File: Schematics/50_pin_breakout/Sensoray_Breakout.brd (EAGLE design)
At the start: 96.2 x 43.8 mm, 26 parts, among them X1 87758-5016

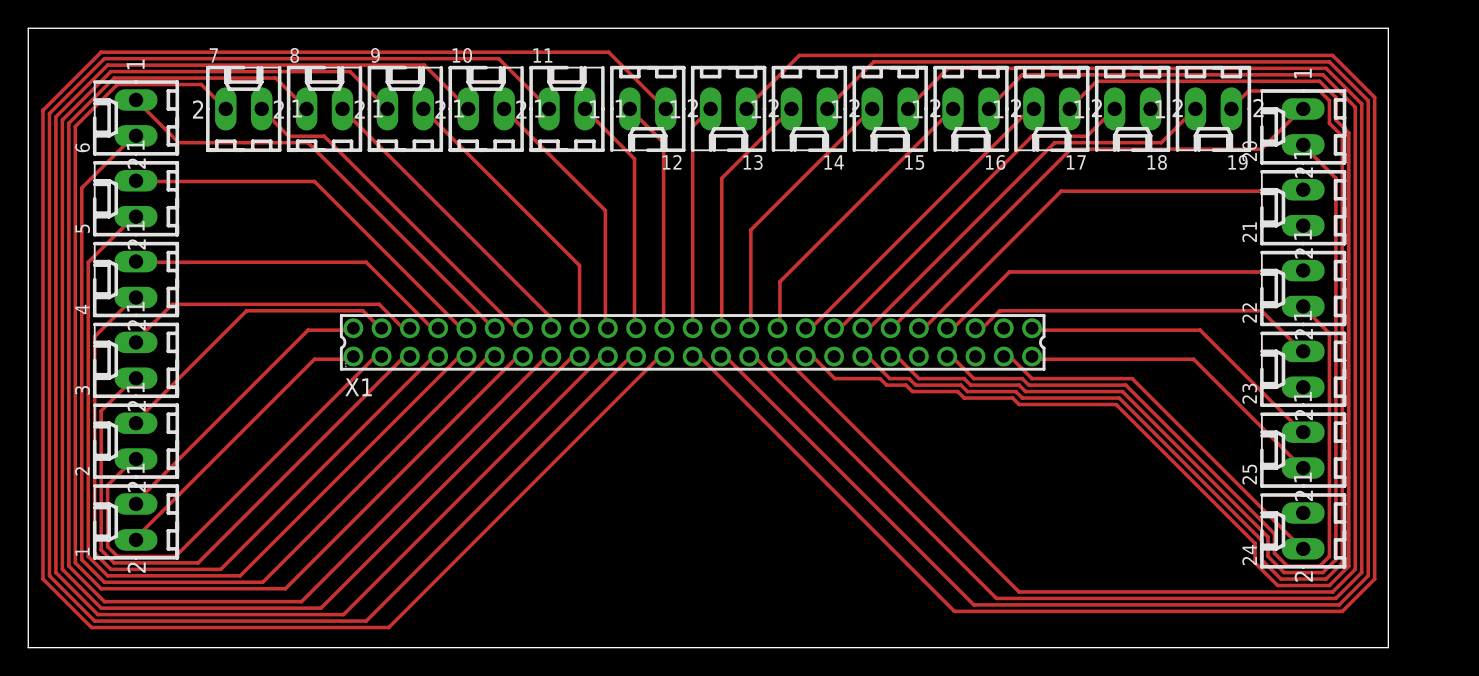
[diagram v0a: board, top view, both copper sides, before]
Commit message: added Rev 2 for 26 and 50 pin breakout boards, along with their gerber files for 1-layer PCB use. also added WPR for week of 27th
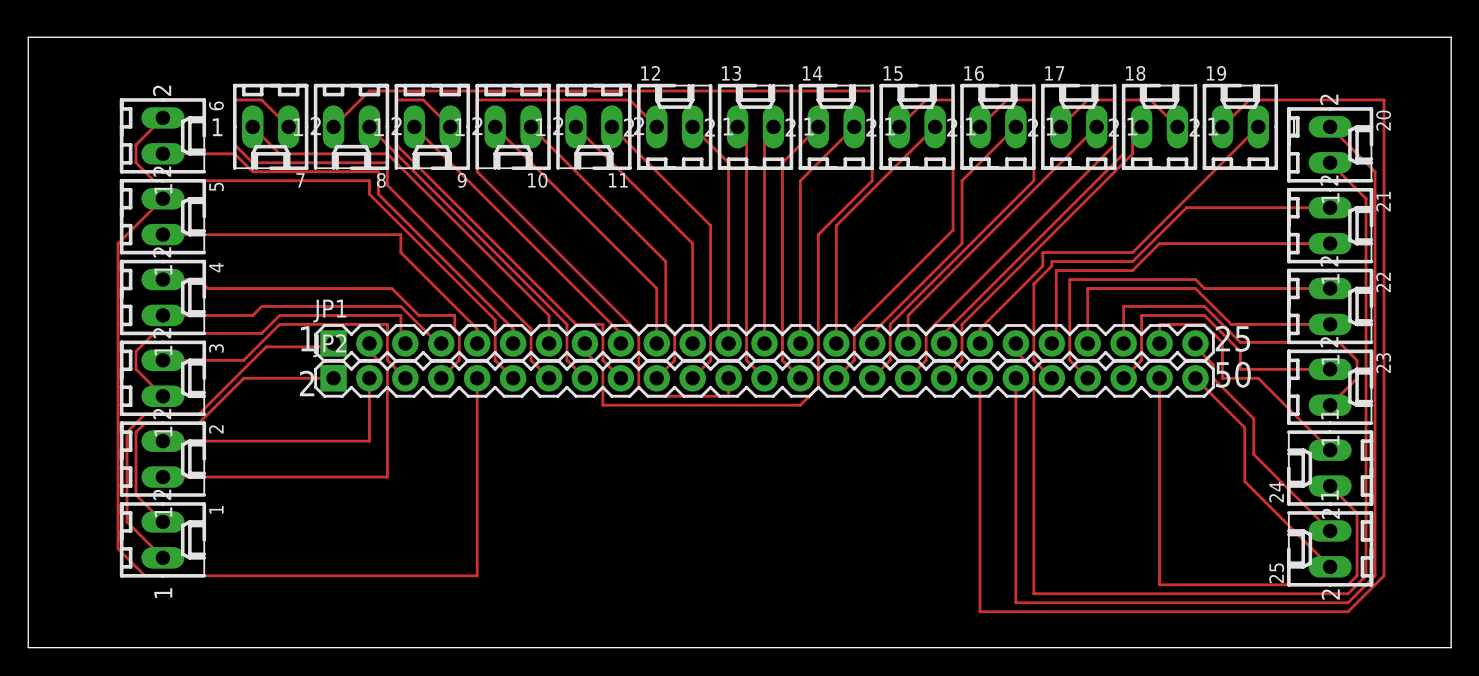
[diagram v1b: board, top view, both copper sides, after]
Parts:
- removed X1: 87758-5016, con-molex:87758-5016
- added JP1, JP2: M25PTH, SparkFun-Connectors:1X25
- moved 25 7.24 mm to (92.1, 6.99)
- moved 24 4.84 mm to (92.1, 12.7)
- moved 10 2.29 mm to (34.3, 36.8), turned to 180 degrees
- moved 11 2.29 mm to (40.0, 36.8), turned to 180 degrees
- moved 12 2.29 mm to (45.7, 36.8), turned to 0 degrees
- moved 13 2.29 mm to (51.4, 36.8), turned to 0 degrees
- moved 14 2.29 mm to (57.1, 36.8), turned to 0 degrees
- moved 15 2.29 mm to (62.9, 36.8), turned to 0 degrees
- moved 16 2.29 mm to (68.6, 36.8), turned to 0 degrees
- moved 17 2.29 mm to (74.3, 36.8), turned to 0 degrees
- moved 18 2.29 mm to (80.0, 36.8), turned to 0 degrees
- moved 19 2.29 mm to (85.7, 36.8), turned to 0 degrees
- moved 8 2.29 mm to (22.9, 36.8), turned to 180 degrees
- moved 6 2.29 mm to (9.53, 36.2), turned to 270 degrees
- moved 21 2.29 mm to (92.1, 29.8), turned to 270 degrees
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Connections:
- net N$1: now also 1.1, JP1.1; no longer 1.2, X1.1
- net N$10: now also 9.1, JP1.9; no longer 8.2, X1.15
- net N$11: now also 25.1, JP1.25; no longer 9.2, X1.17
- net N$12: now also 24.1, JP1.24; no longer 10.2, X1.19
- net N$13: now also 23.1, JP1.23; no longer 11.2, X1.21
- net N$14: now also 22.1, JP1.22; no longer 12.2, X1.23
- net N$15: now also 21.1, JP1.21; no longer 13.2, X1.25
- net N$16: now also 20.1, JP1.20; no longer 3.1, X1.6
- net N$17: now also 19.1, JP1.19; no longer 4.1, X1.8
- net N$18: now also 18.1, JP1.18; no longer 5.1, X1.10
- net N$19: now also 17.1, JP1.17; no longer 6.1, X1.12
- net N$2: now also 2.1, JP1.2; no longer 1.1, X1.2
- net N$20: now also 16.1, JP1.16; no longer 7.1, X1.14
- net N$21: now also 15.1, JP1.15; no longer 8.1, X1.16
- net N$22: now also 14.1, JP1.14; no longer 9.1, X1.18
- net N$23: now also 13.1, JP1.13; no longer 10.1, X1.20
- net N$24: now also 12.1, JP1.12; no longer 11.1, X1.22
- net N$25: now also 11.1, JP1.11; no longer 12.1, X1.24
- net N$26: now also 10.1, JP1.10; no longer 13.1, X1.26
- net N$27: now also 1.2, JP2.1; no longer 14.2, X1.27
- net N$28: now also 3.2, JP2.3; no longer 15.2, X1.29
- net N$29: now also 4.2, JP2.4; no longer 16.2, X1.31
- net N$3: now also JP2.2; no longer X1.3
- net N$30: now also 5.2, JP2.5; no longer 17.2, X1.33
- net N$31: now also 6.2, JP2.6; no longer 18.2, X1.35
- net N$32: now also 7.2, JP2.7; no longer 19.2, X1.37
- net N$33: now also 8.2, JP2.8; no longer 20.2, X1.39
- net N$34: now also 9.2, JP2.9; no longer 21.2, X1.41
- net N$35: now also 10.2, JP2.10; no longer 22.2, X1.43
- net N$36: now also 11.2, JP2.11; no longer 23.2, X1.45
- net N$37: now also 12.2, JP2.12; no longer 24.2, X1.47
- net N$38: now also 13.2, JP2.13; no longer 25.2, X1.49
- net N$39: now also 14.2, JP2.14; no longer 14.1, X1.28
- net N$4: now also 3.1, JP1.3; no longer 2.1, X1.4
- net N$40: now also 15.2, JP2.15; no longer 15.1, X1.30
- net N$41: now also 16.2, JP2.16; no longer 16.1, X1.32
- net N$42: now also 17.2, JP2.17; no longer 17.1, X1.34
- net N$43: now also 18.2, JP2.18; no longer 18.1, X1.36
- net N$44: now also 19.2, JP2.19; no longer 19.1, X1.38
- net N$45: now also 20.2, JP2.20; no longer 20.1, X1.40
- net N$46: now also 21.2, JP2.21; no longer 21.1, X1.42
- net N$47: now also 22.2, JP2.22; no longer 22.1, X1.44
- net N$48: now also 23.2, JP2.23; no longer 23.1, X1.46
- net N$49: now also 24.2, JP2.24; no longer 24.1, X1.48
- net N$5: now also 4.1, JP1.4; no longer 3.2, X1.5
- net N$50: now also 25.2, JP2.25; no longer 25.1, X1.50
- net N$6: now also 5.1, JP1.5; no longer 4.2, X1.7
- net N$7: now also 6.1, JP1.6; no longer 5.2, X1.9
- net N$8: now also 7.1, JP1.7; no longer 6.2, X1.11
- net N$9: now also 8.1, JP1.8; no longer 7.2, X1.13
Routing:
- net N$15: track 138.1 -> 25.4 mm
- net N$14: track 133.9 -> 22.1 mm
- net N$27: track 128.4 -> 22.7 mm
- net N$28: track 118.7 -> 21.3 mm
- net N$13: track 121.7 -> 24.7 mm
- net N$12: track 112.0 -> 18.6 mm
- net N$11: track 102.5 -> 17.2 mm
- net N$29: track 109.0 -> 26.8 mm
- net N$10: track 92.8 -> 21.4 mm
- net N$44: track 30.0 -> 92.0 mm
- net N$16: track 21.2 -> 72.5 mm
- net N$33: track 69.3 -> 24.1 mm
- net N$32: track 82.6 -> 39.1 mm
- net N$8: track 68.1 -> 28.5 mm
- net N$45: track 35.6 -> 75.1 mm
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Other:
- board size 96.2 x 43.8 mm -> 100.6 x 43.2 mm
- board text added: "1"
- board text added: "2"
- board text added: "25"
- board text added: "50"

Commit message: adding v3 of 50 pin board. fixed the pins flipping in the center of the board.
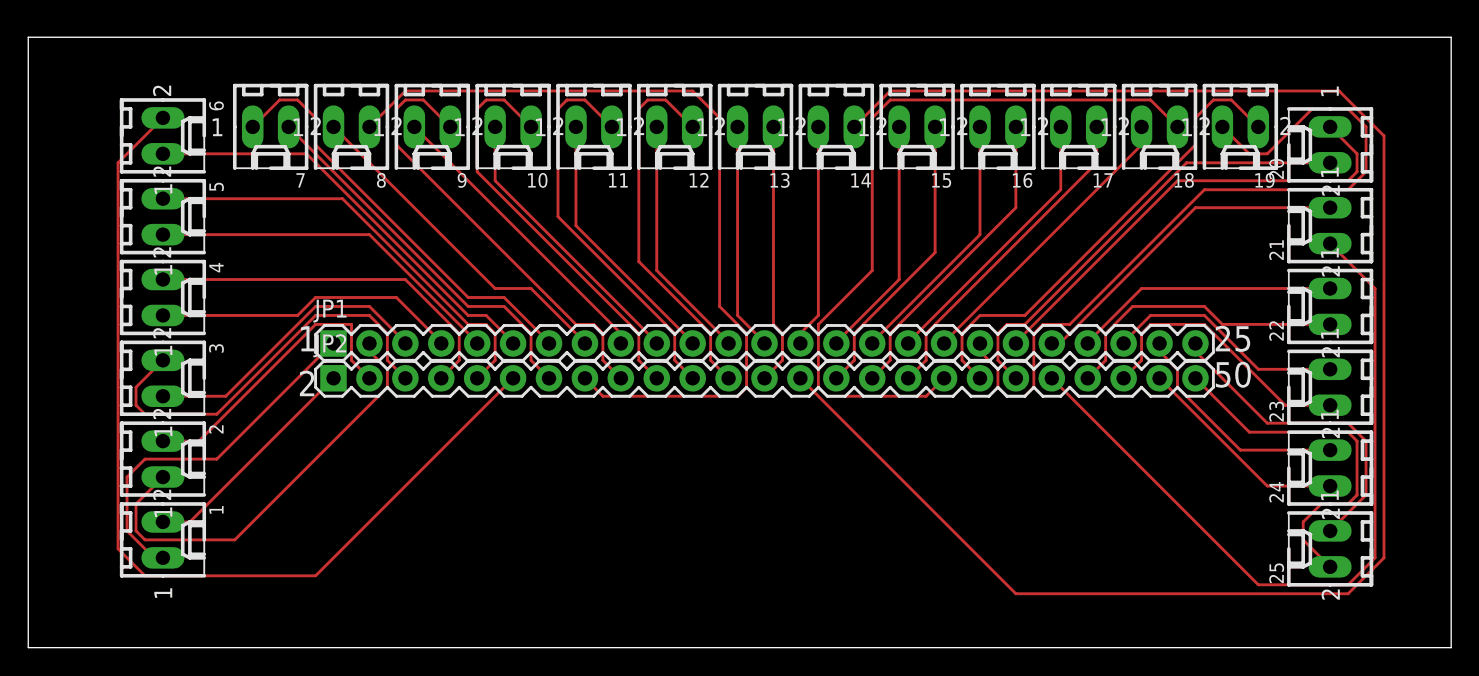
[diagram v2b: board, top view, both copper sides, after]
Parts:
- turned 12 to 180 degrees
- turned 13 to 180 degrees
- turned 14 to 180 degrees
- turned 15 to 180 degrees
- turned 16 to 180 degrees
- turned 17 to 180 degrees
- turned 18 to 180 degrees
- turned 19 to 180 degrees
- turned 20 to 90 degrees
- turned 21 to 90 degrees
- turned 22 to 90 degrees
- turned 23 to 90 degrees
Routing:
- net N$39: track 19.4 -> 118.3 mm
- net N$44: track 92.0 -> 33.4 mm
- net N$9: track 82.3 -> 24.2 mm
- net N$45: track 75.1 -> 32.2 mm
- net N$16: track 72.5 -> 33.2 mm
- net N$30: track 66.2 -> 31.1 mm
- net N$33: track 24.1 -> 58.7 mm
- net N$43: track 23.6 -> 53.2 mm
- net N$17: track 27.2 -> 54.7 mm
- net N$31: track 39.2 -> 66.3 mm
- net N$46: track 30.6 -> 53.2 mm
- net N$49: track 36.0 -> 15.2 mm
- net N$37: track 46.4 -> 26.5 mm
- net N$32: track 39.1 -> 26.9 mm
- net N$50: track 17.3 -> 25.6 mm
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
